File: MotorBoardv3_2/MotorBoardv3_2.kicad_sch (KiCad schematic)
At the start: 84 parts, among them J1 Bump0, J10 RxD, J11 GP2Y0A41SK0F, J12 GP2Y0A41SK0F, J13 GP2Y0A41SK0F, J14 TxD, J15 7.2, J16 LP5.0, J17 ELA, J18 ERA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

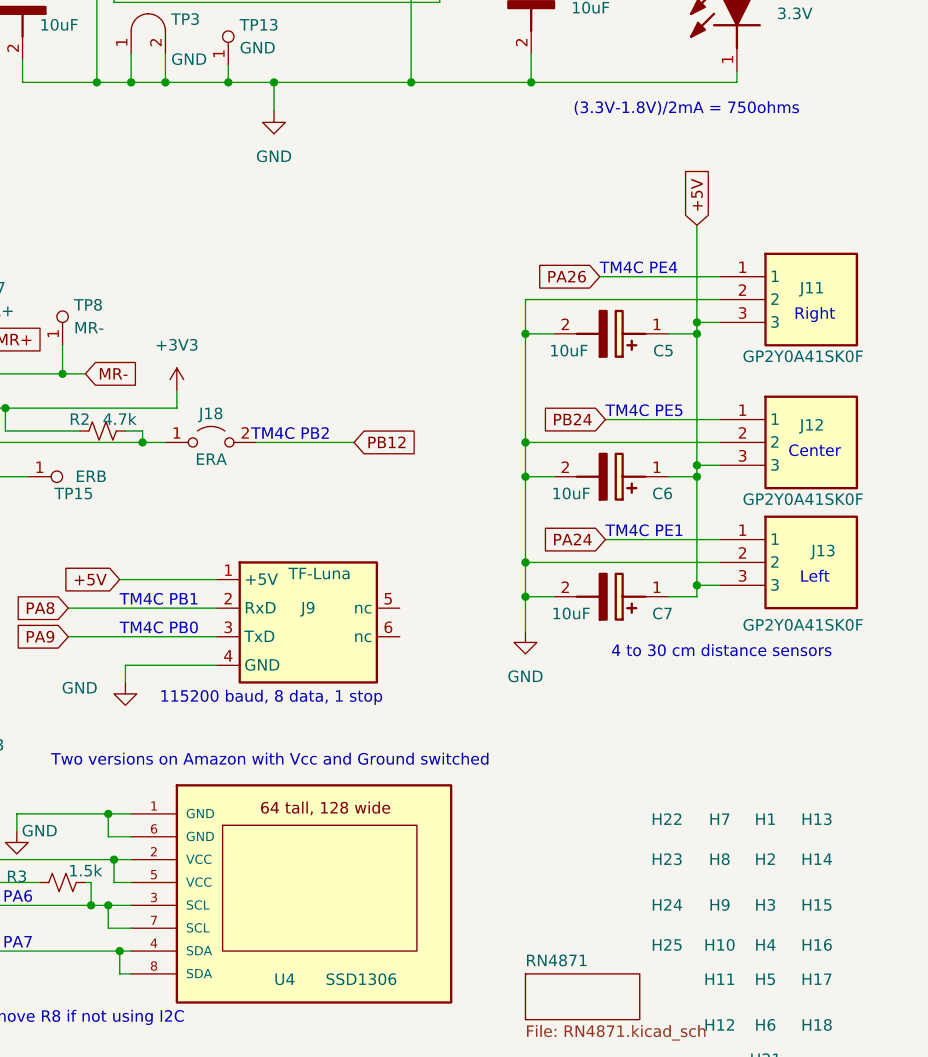
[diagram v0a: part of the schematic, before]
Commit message: Completed Schematic w/ charge circuit, voltmeter, bluetooth, Reflective Sensor Port
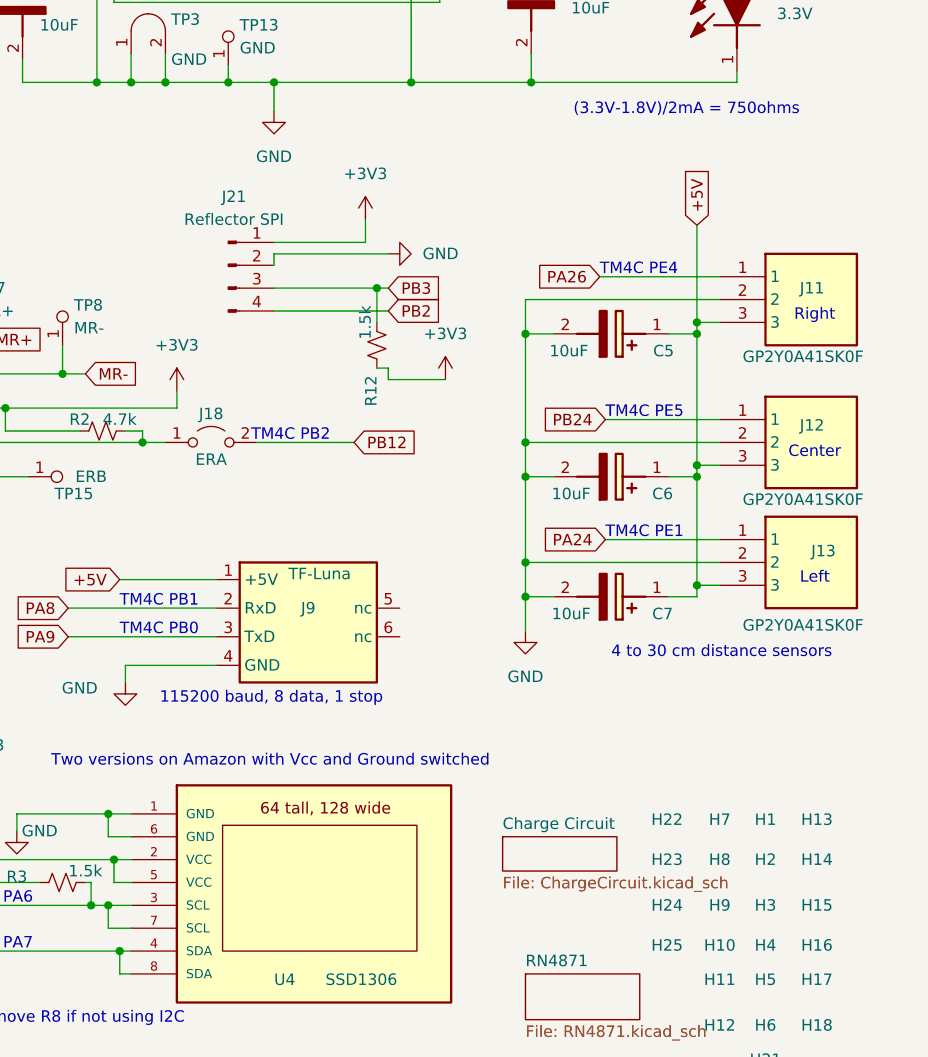
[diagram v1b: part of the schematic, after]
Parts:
- added J21: Reflector SPI, Connector_PinHeader_2.54mm:PinHeader_1x04_P2.54mm_Vertical, symbol Connector:Conn_01x04_Pin
- added R12: 1.5k, RSLK2:R_0603_1608Metric, symbol RSLK2:R_0603_1500
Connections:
- net +3V3: now also J21.1 (Pin_1), R12.1
- net GND: now also J21.2 (Pin_2)
- net PB2: now also J21.4 (Pin_4)
- net PB3: now also J21.3 (Pin_3), R12.2
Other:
- added sheet Charge Circuit (ChargeCircuit.kicad_sch)

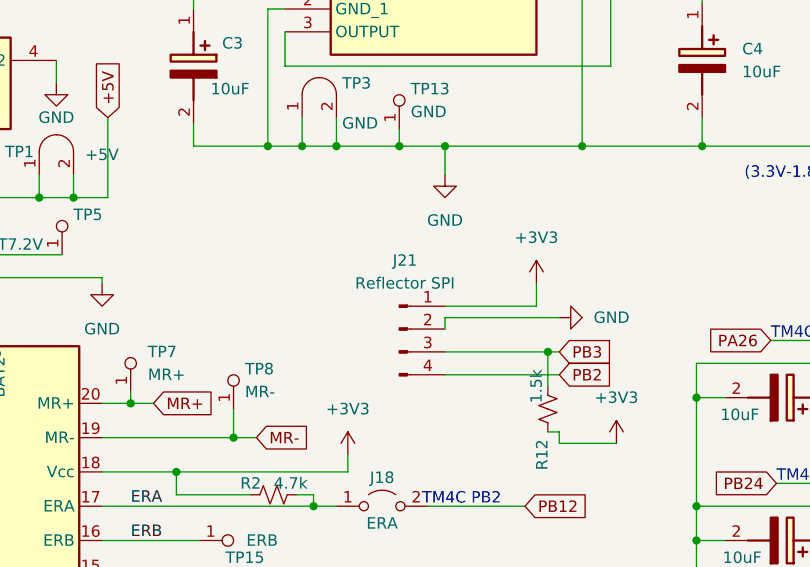
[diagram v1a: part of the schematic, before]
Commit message: corrected david's silly label
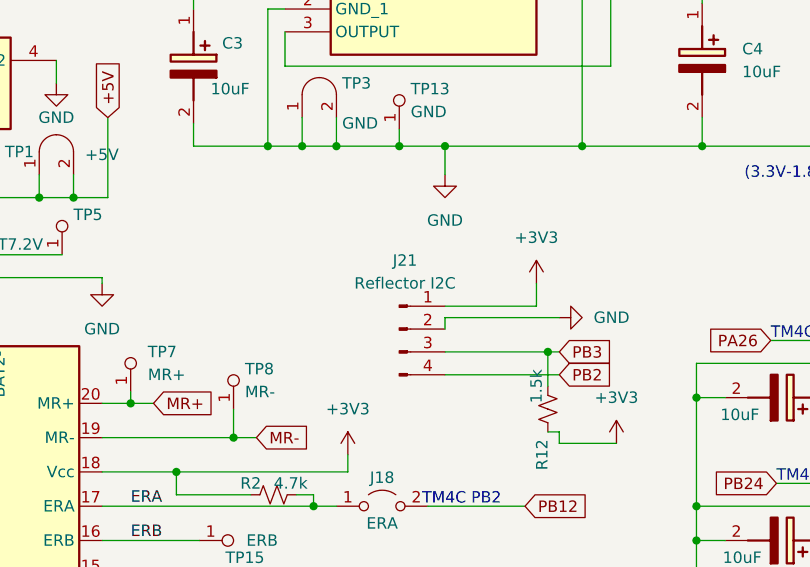
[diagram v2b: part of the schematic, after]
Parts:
- J21: value Reflector SPI -> Reflector I2C
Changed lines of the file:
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@@
 	(label "ELB"
 		(at 133.35 97.155 0)
+		(fields_autoplaced yes)
 		(effects
 			(font
@@
 	(label "ESP_RxD"
 		(at 89.535 119.38 0)
+		(fields_autoplaced yes)
 		(effects
 			(font
@@
 	(label "ELA"
 		(at 138.43 93.345 0)
+		(fields_autoplaced yes)
 		(effects
 			(font
@@
 	(label "ERA"
 		(at 183.515 93.345 0)
+		(fields_autoplaced yes)
 		(effects
 			(font
@@
 	(label "Ch_PD"
 		(at 121.285 125.73 0)
+		(fields_autoplaced yes)
 		(effects
 			(font
@@
 	(label "LP3_3"
 		(at 20.32 24.13 0)
+		(fields_autoplaced yes)
 		(effects
 			(font
@@
 	(label "ERB"
 		(at 183.515 97.155 0)
+		(fields_autoplaced yes)
 		(effects
 			(font
@@
 	(label "VBUS"
 		(at 48.895 19.05 0)
+		(fields_autoplaced yes)
 		(effects
 			(font
@@
 	(label "ESP_TxD"
 		(at 120.65 128.905 0)
+		(fields_autoplaced yes)
 		(effects
 			(font
@@
 			)
 		)
-		(property "Value" "Reflector SPI"
+		(property "Value" "Reflector I2C"
 			(at 213.995 68.58 0)
 			(effects

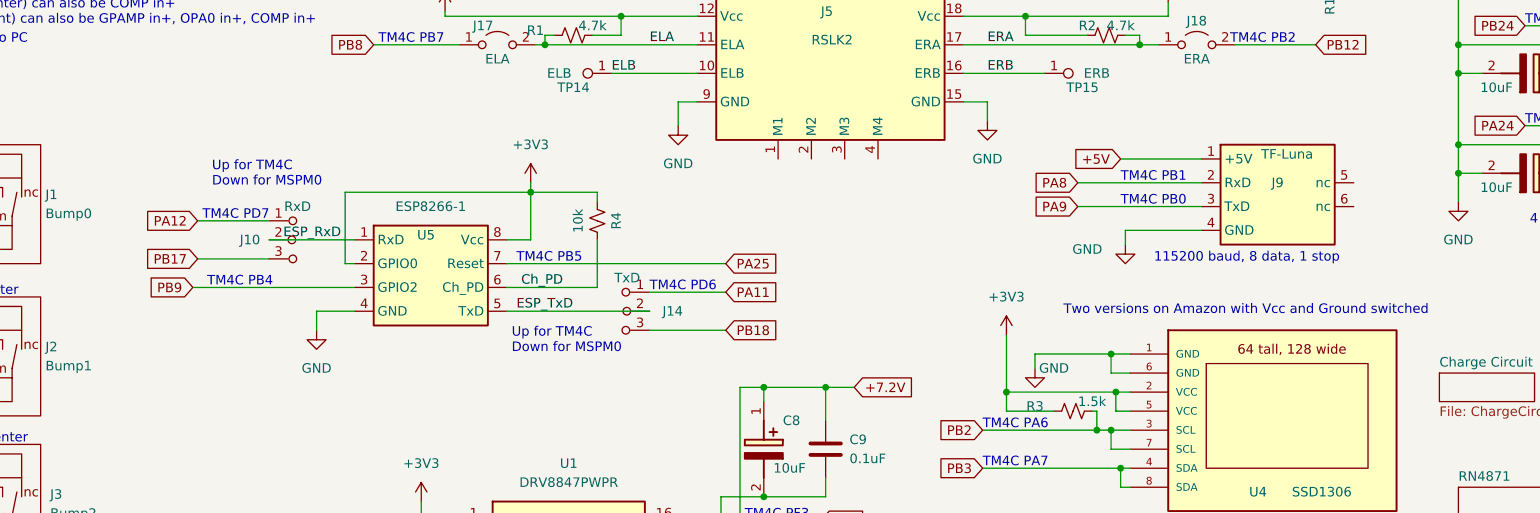
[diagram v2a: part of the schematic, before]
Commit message: deleted esp8266 and tf-luna circuits from schematic
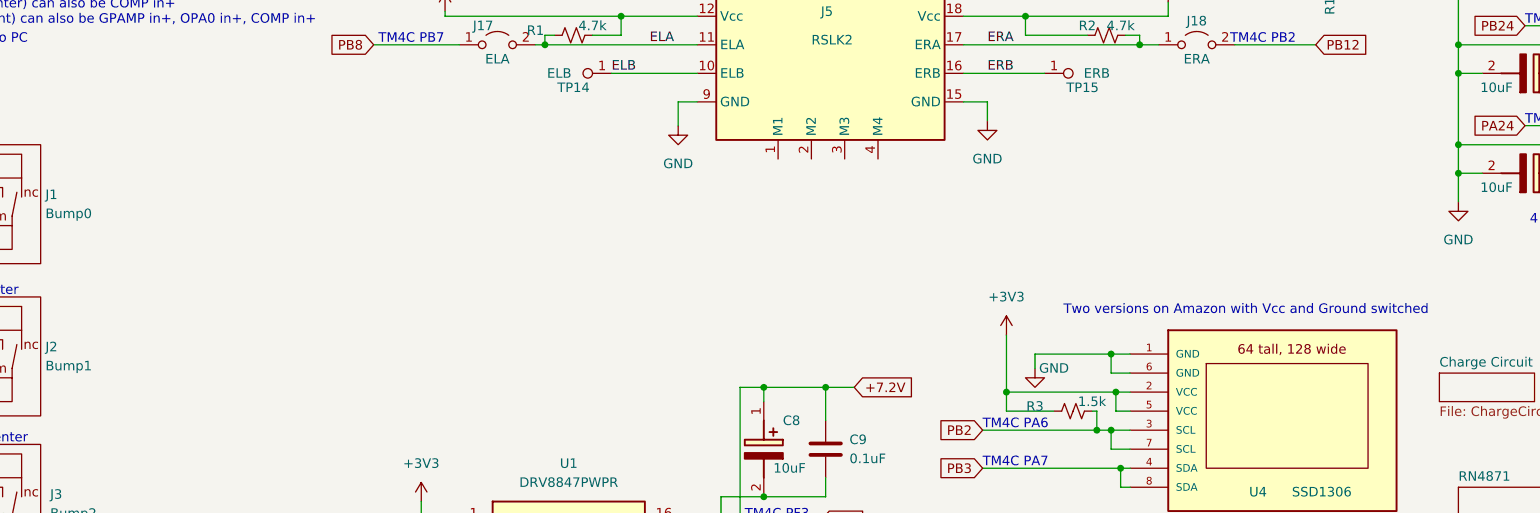
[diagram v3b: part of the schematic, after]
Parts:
- removed J10: RxD, RSLK2:PinHeader_1x03_P2.54mm_Vertical, symbol RSLK2:Header_3
- removed J14: TxD, RSLK2:PinHeader_1x03_P2.54mm_Vertical, symbol RSLK2:Header_3
- removed J9: TF-Luna, RSLK2:JST-GH_1x06_1.25mm, symbol RSLK2:TF-Luna
- removed R4: 10k, RSLK2:R_0603_1608Metric, symbol RSLK2:R_0603
- removed U5: ESP8266-1, RSLK2:PinHeader_2x04_P2.54mm_Vertical, symbol RSLK2:ESP8266-1
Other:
- note removed: "115200 baud, 8 data, 1 stop"
- note removed: "TM4C PB0"
- note removed: "TM4C PB1"
- note removed: "TM4C PB4"
- note removed: "TM4C PB5"
- note removed: "TM4C PD6"
- note removed: "TM4C PD7"
- note removed: "Up for TM4C Down for MSPM0"

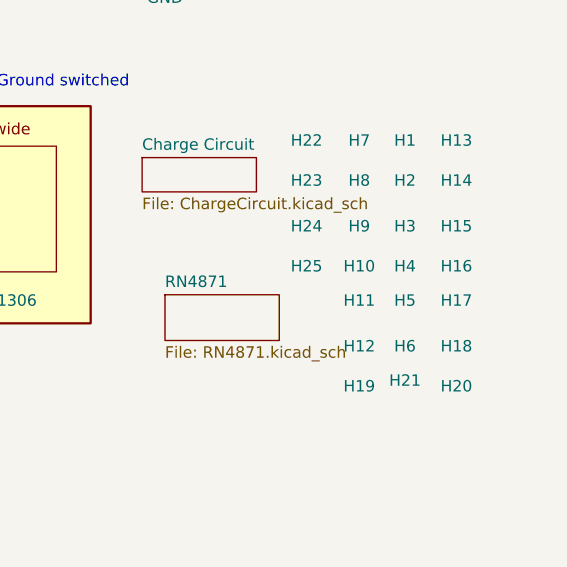
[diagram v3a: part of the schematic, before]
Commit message: routed RN4871 eval board pins
Also changed the positions of some silkscreen labels
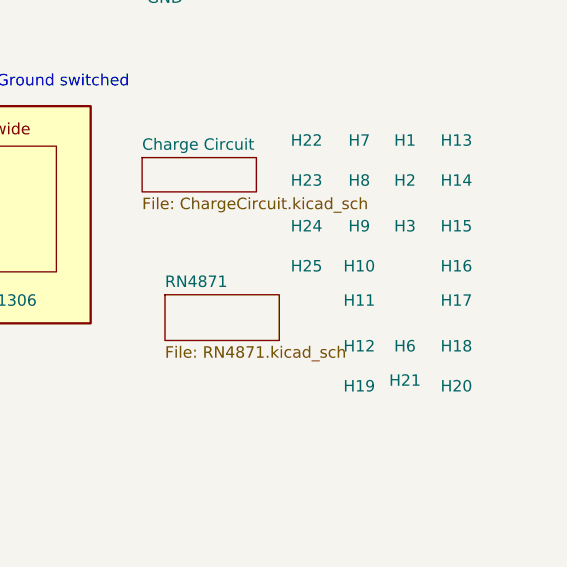
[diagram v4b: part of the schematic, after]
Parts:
- removed H4, H5: ~, RSLK2:MountingHole_4_40, symbol RSLK2:MountingHole
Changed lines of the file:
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@@
 	)
 	(symbol
-		(lib_id "RSLK2:MountingHole")
-		(at 260.35 155.575 0)
-		(unit 1)
-		(exclude_from_sim no)
-		(in_bom yes)
-		(on_board yes)
-		(dnp no)
-		(property "Reference" "H5"
-			(at 273.05 153.035 0)
-			(effects
-				(font
-					(size 1.27 1.27)
-				)
-			)
-		)
-		(property "Value" "~"
-			(at 260.35 155.575 0)
-			(effects
-				(font
-					(size 1.27 1.27)
-				)
-			)
-		)
-		(property "Footprint" "RSLK2:MountingHole_4_40"
-			(at 260.35 155.575 0)
-			(effects
-				(font
-					(size 1.27 1.27)
-				)
-				(hide yes)
-			)
-		)
-		(property "Datasheet" ""
-			(at 260.35 155.575 0)
-			(effects
-				(font
-					(size 1.27 1.27)
-				)
-				(hide yes)
-			)
-		)
-		(property "Description" "Drill hole for 4-40 screw"
-			(at 260.35 155.575 0)
-			(effects
-				(font
-					(size 1.27 1.27)
-				)
-				(hide yes)
-			)
-		)
-		(instances
-			(project "MotorBoardv3_2"
-				(path "/69b823fd-c065-40ff-9bb9-c5835555f3eb"
-					(reference "H5")
-					(unit 1)
-				)
-			)
-		)
-	)
-	(symbol
 		(lib_id "RSLK2:Testpoint_1")
 		(at 127 81.915 0)
@@
 		(on_board yes)
 		(dnp no)
-		(fields_autoplaced yes)
 		(property "Reference" "C9"
 			(at 165.1 146.05 0)
@@
 		(on_board yes)
 		(dnp no)
-		(fields_autoplaced yes)
 		(property "Reference" "H10"
 			(at 267.97 149.225 0)
@@
 					(unit 1)
 				)
-			)
-		)
-	)
-	(symbol
-		(lib_id "RSLK2:MountingHole")
-		(at 260.35 151.765 0)
-		(unit 1)
-		(exclude_from_sim no)
-		(in_bom yes)
-		(on_board yes)
-		(dnp no)
-		(property "Reference" "H4"
-			(at 273.05 149.225 0)
-			(effects
-				(font
-					(size 1.27 1.27)
-				)
-			)
-		)
-		(property "Value" "~"
-			(at 260.35 151.765 0)
-			(effects
-				(font
-					(size 1.27 1.27)
-				)
-			)
-		)
-		(property "Footprint" "RSLK2:MountingHole_4_40"
-			(at 260.35 151.765 0)
-			(effects
-				(font
-					(size 1.27 1.27)
-				)
-				(hide yes)
-			)
-		)
-		(property "Datasheet" ""
-			(at 260.35 151.765 0)
-			(effects
-				(font
-					(size 1.27 1.27)
-				)
-				(hide yes)
-			)
-		)
-		(property "Description" "Drill hole for 4-40 screw"
-			(at 260.35 151.765 0)
-			(effects
-				(font
-					(size 1.27 1.27)
-				)
-				(hide yes)
-			)
-		)
-		(instances
-			(project "MotorBoardv3_2"
-				(path "/69b823fd-c065-40ff-9bb9-c5835555f3eb"
-					(reference "H4")
-					(unit 1)
-				)
